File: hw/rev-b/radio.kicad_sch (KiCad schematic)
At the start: 70 parts, among them Q101 SIA975DJ-T1-GE3, Q102 2N7002, U101 TPS2116DRLR, U102 TPS2553DBVR, U103 TPS63802DLAR, U104 ESP32-C3-MINI-1U-N4, U105 SN74LVC1G125DBVR, U106 SN74LVC3G34DCTR, U107 CH334P, U108 TLV3012BIDBVR, U109 TLV431BIDBZR, Y101 12MHz 10pF 10ppm

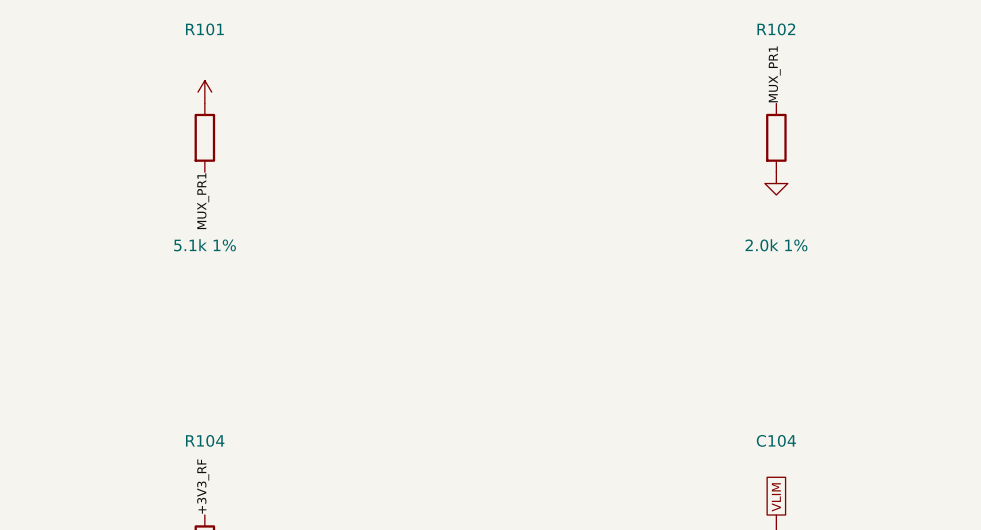
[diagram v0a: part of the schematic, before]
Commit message: R101/R102 1.3k/510: same USB threshold, 3x D3-leakage margin; BOM/CPL regenerated; all gates re-run
Co-Authored-By: Claude Opus 5.5 (1M context) <noreply@anthropic.com>
Claude-Session: https://claude.ai/code/session_01F5zMMQgMFiMCad54U85DYT
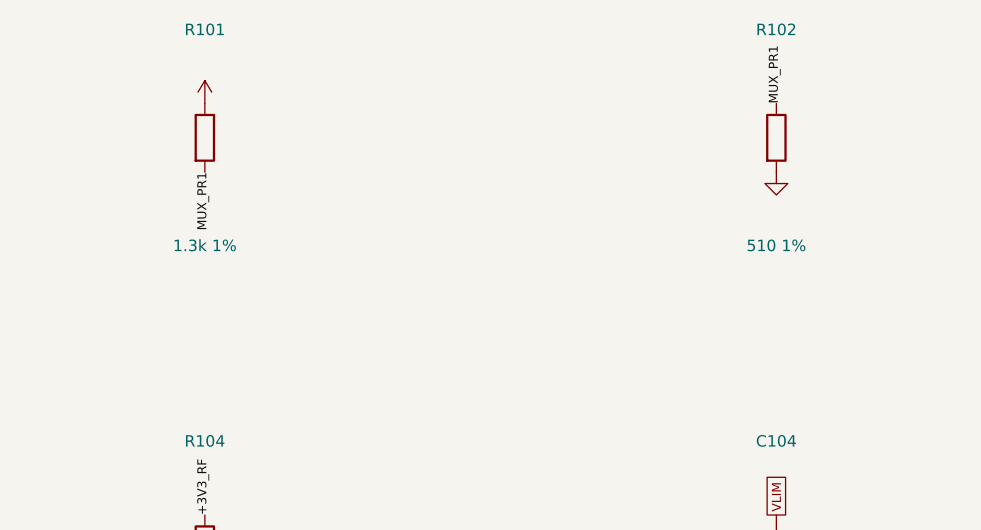
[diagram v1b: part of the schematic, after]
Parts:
- R101: value 5.1k 1% -> 1.3k 1%; LCSC C25905 -> C25866
- R102: value 2.0k 1% -> 510 1%; LCSC C4109 -> C25123
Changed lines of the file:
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@@
 			)
 		)
-		(property "Value" "5.1k 1%"
+		(property "Value" "1.3k 1%"
 			(at 88.9 57.72 0)
 			(effects
@@
 			)
 		)
-		(property "LCSC" "C25905"
+		(property "LCSC" "C25866"
 			(at 88.9 45.72 0)
 			(effects
@@
 			)
 		)
-		(property "Value" "2.0k 1%"
+		(property "Value" "510 1%"
 			(at 152.4 57.72 0)
 			(effects
@@
 			)
 		)
-		(property "LCSC" "C4109"
+		(property "LCSC" "C25123"
 			(at 152.4 45.72 0)
 			(effects

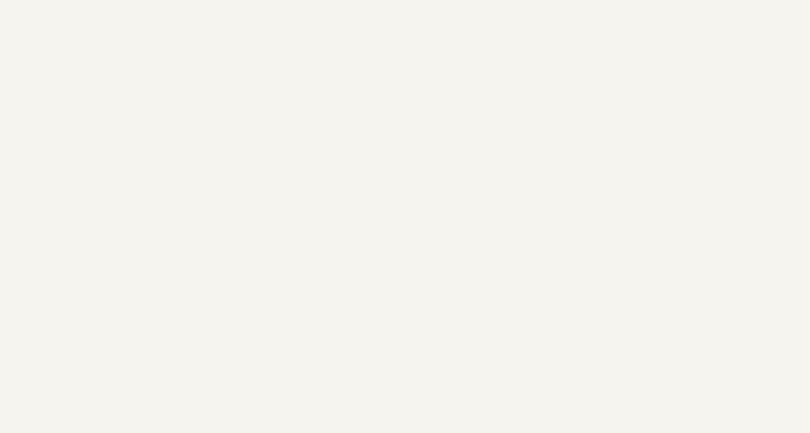
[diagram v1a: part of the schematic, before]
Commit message: Rev B: fixes from the wallet cart's JLC check and datasheet review
- JLC gate (verify/jlc_check.py): top-edge GND vias 0.06 mm inward, copper-to-edge
  rule 0.2 mm with a J5 exemption (.kicad_dru), back URL/credit text 1.0 mm. PASS.
- Radio-area ground: F.Cu GND pour, 56 stitching vias, one via per U104 centre
  sub-pad, vias at U103 GND pins, C106, U106.4. GND vias 214 -> 285.
- RP2350 VREG_LX keepout on In1-In4; DEBUG_UART_TX and LED_DIN rerouted around it.
- R110 -> C453777 (C4147 below JLC's minimum buy); make_bom now checks minimum buy.
- R133 4.7k GBBUS_EN pull-down (TXB0108 OE).
- Y1 -> ABM8-272-T3 C20625731.
- USB upstream D+ moved onto In2 with D-: 2 vias each, 12.42 / 11.84 mm.
- All gates re-run; BOM/CPL/Gerbers/zip/renders regenerated. LOGBOOK 2026-10-16 12:15.

Co-Authored-By: Claude Opus 5.5 (1M context) <noreply@anthropic.com>
Claude-Session: https://claude.ai/code/session_01F5zMMQgMFiMCad54U85DYT
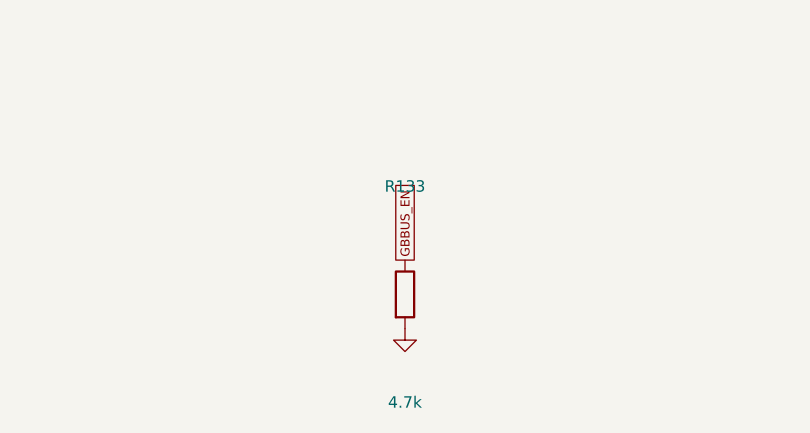
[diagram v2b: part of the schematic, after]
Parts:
- added R133: 4.7k, Resistor_SMD:R_0402_1005Metric, symbol Device:R
- R110: LCSC C4147 -> C453777
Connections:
- net GND: now also R133.2
- new net GBBUS_EN: R133.1
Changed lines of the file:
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@@
 			)
 		)
-		(property "LCSC" "C4147"
+		(property "LCSC" "C453777"
 			(at 88.9 172.72 0)
 			(effects
@@
 			)
 		)
+	)
+	(global_label "GBBUS_EN"
+		(shape passive)
+		(at 88.9 544.83 90)
+		(fields_autoplaced yes)
+		(effects
+			(font
+				(size 1.0 1.0)
+			)
+			(justify left)
+		)
+		(property "Intersheetrefs" "${INTERSHEET_REFS}"
+			(at 88.9 544.83 0)
+			(effects
+				(font
+					(size 1.0 1.0)
+				)
+				(hide yes)
+			)
+		)
+	)
+	(symbol
+		(lib_id "power:GND")
+		(at 88.9 552.45 0)
+		(unit 1)
+		(exclude_from_sim no)
+		(in_bom yes)
+		(on_board yes)
+		(dnp no)
+		(property "Reference" "#PWR01081"
+			(at 88.9 557.45 0)
+			(effects
+				(font
+					(size 1.27 1.27)
+				)
+				(hide yes)
+			)
+		)
+		(property "Value" "GND"
+			(at 88.9 555.45 0)
+			(effects
+				(font
+					(size 1.27 1.27)
+				)
+				(hide yes)
+			)
+		)
+		(property "Footprint" ""
+			(at 88.9 552.45 0)
+			(effects
+				(font
+					(size 1.27 1.27)
+				)
+				(hide yes)
+			)
+		)
+		(property "Datasheet" ""
+			(at 88.9 552.45 0)
+			(effects
+				(font
+					(size 1.27 1.27)
+				)
+				(hide yes)
+			)
+		)
+		(property "Description" ""
+			(at 88.9 552.45 0)
+			(effects
+				(font
+					(size 1.27 1.27)
+				)
+				(hide yes)
+			)
+		)
+		(pin "1"
+		)
+		(instances
+			(project "GameboyCartridgeV2.1"
+				(path "/ec16e1da-c950-4911-941a-a1ab0200cc01/5f3a9c2e-7b1d-4e6a-9c0f-1a2b3c4d5e60"
+					(reference "#PWR01081")
+					(unit 1)
+				)
+			)
+		)
+	)
+	(symbol
+		(lib_id "Device:R")
+		(at 88.9 548.64 0)
+		(unit 1)
+		(exclude_from_sim no)
+		(in_bom yes)
+		(on_board yes)
+		(dnp no)
+		(property "Reference" "R133"
+			(at 88.9 536.64 0)
+			(effects
+				(font
+					(size 1.27 1.27)
+				)
+			)
+		)
+		(property "Value" "4.7k"
+			(at 88.9 560.64 0)
+			(effects
+				(font
+					(size 1.27 1.27)
+				)
+			)
+		)
+		(property "Footprint" "Resistor_SMD:R_0402_1005Metric"
+			(at 88.9 548.64 0)
+			(effects
+				(font
+					(size 1.27 1.27)
+				)
+				(hide yes)
+			)
+		)
+		(property "Datasheet" ""
+			(at 88.9 548.64 0)
+			(effects
+				(font
+					(size 1.27 1.27)
+				)
+				(hide yes)
+			)
+		)
+		(property "Description" ""
+			(at 88.9 548.64 0)
+			(effects
+				(font
+					(size 1.27 1.27)
+				)
+				(hide yes)
+			)
+		)
+		(property "LCSC" "C25900"
+			(at 88.9 548.64 0)
+			(effects
+				(font
+					(size 1.27 1.27)
+				)
+				(hide yes)
+			)
+		)
+		(pin "1"
+		)
+		(pin "2"
+		)
+		(instances
+			(project "GameboyCartridgeV2.1"
+				(path "/ec16e1da-c950-4911-941a-a1ab0200cc01/5f3a9c2e-7b1d-4e6a-9c0f-1a2b3c4d5e60"
+					(reference "R133")
+					(unit 1)
+				)
+			)
+		)

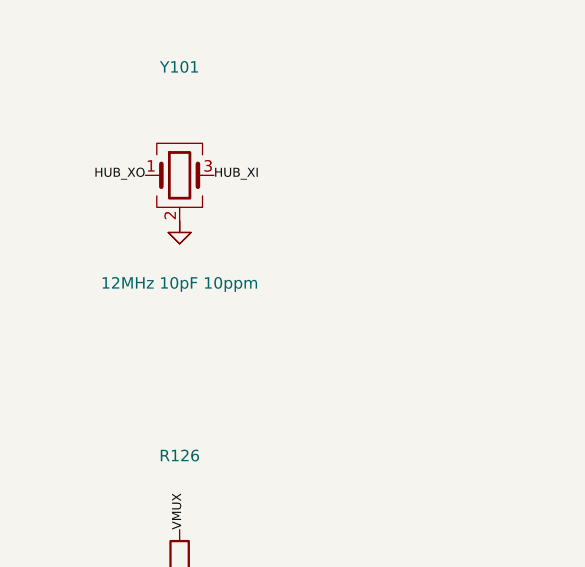
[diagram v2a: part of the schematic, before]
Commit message: Y101 hub crystal -> ABM8-272-T3, same part as Y1
CH334 datasheet gives no ESR limit (only ~16 pF internal load, 12 MHz), so the
old part was within spec; swapped for 50 ohm ESR margin and one feeder fewer.
Gates re-run, LOGBOOK 2026-10-16 12:35.

Co-Authored-By: Claude Opus 5.5 (1M context) <noreply@anthropic.com>
Claude-Session: https://claude.ai/code/session_01F5zMMQgMFiMCad54U85DYT
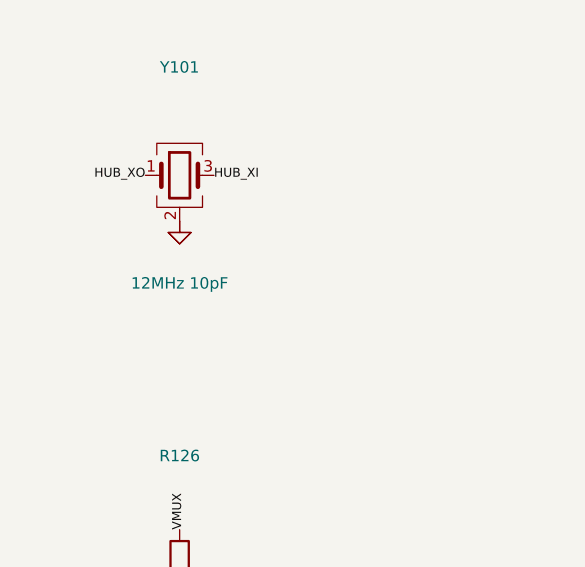
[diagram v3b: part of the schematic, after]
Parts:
- Y101: value 12MHz 10pF 10ppm -> 12MHz 10pF; LCSC C668845 -> C20625731
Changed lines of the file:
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@@
 			)
 		)
-		(property "Value" "12MHz 10pF 10ppm"
+		(property "Value" "12MHz 10pF"
 			(at 25.4 365.06 0)
 			(effects
@@
 			)
 		)
-		(property "LCSC" "C668845"
+		(property "LCSC" "C20625731"
 			(at 25.4 353.06 0)
 			(effects
